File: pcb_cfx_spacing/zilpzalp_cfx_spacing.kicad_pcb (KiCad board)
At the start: 2 copper layers, 205.1 x 102.2 mm, 43 parts, among them SW1 SW_Push, SW10 SW_Push, SW11 SW_Push, SW12 SW_Push, SW13 SW_Push, SW14 SW_Push, SW15 SW_Push, SW16 SW_Push, SW17 SW_Push, SW18 SW_Push, SW19 SW_Push, SW2 SW_Push, SW20 SW_Push, SW21 SW_Push, SW22 SW_Push, SW23 SW_Push, SW24 SW_Push, SW25 SW_Push, SW26 SW_Push, SW27 SW_Push, SW28 SW_Push, SW3 SW_Push, SW4 SW_Push, SW5 SW_Push, SW6 SW_Push, SW7 SW_Push, SW8 SW_Push, SW9 SW_Push, U1 xiao

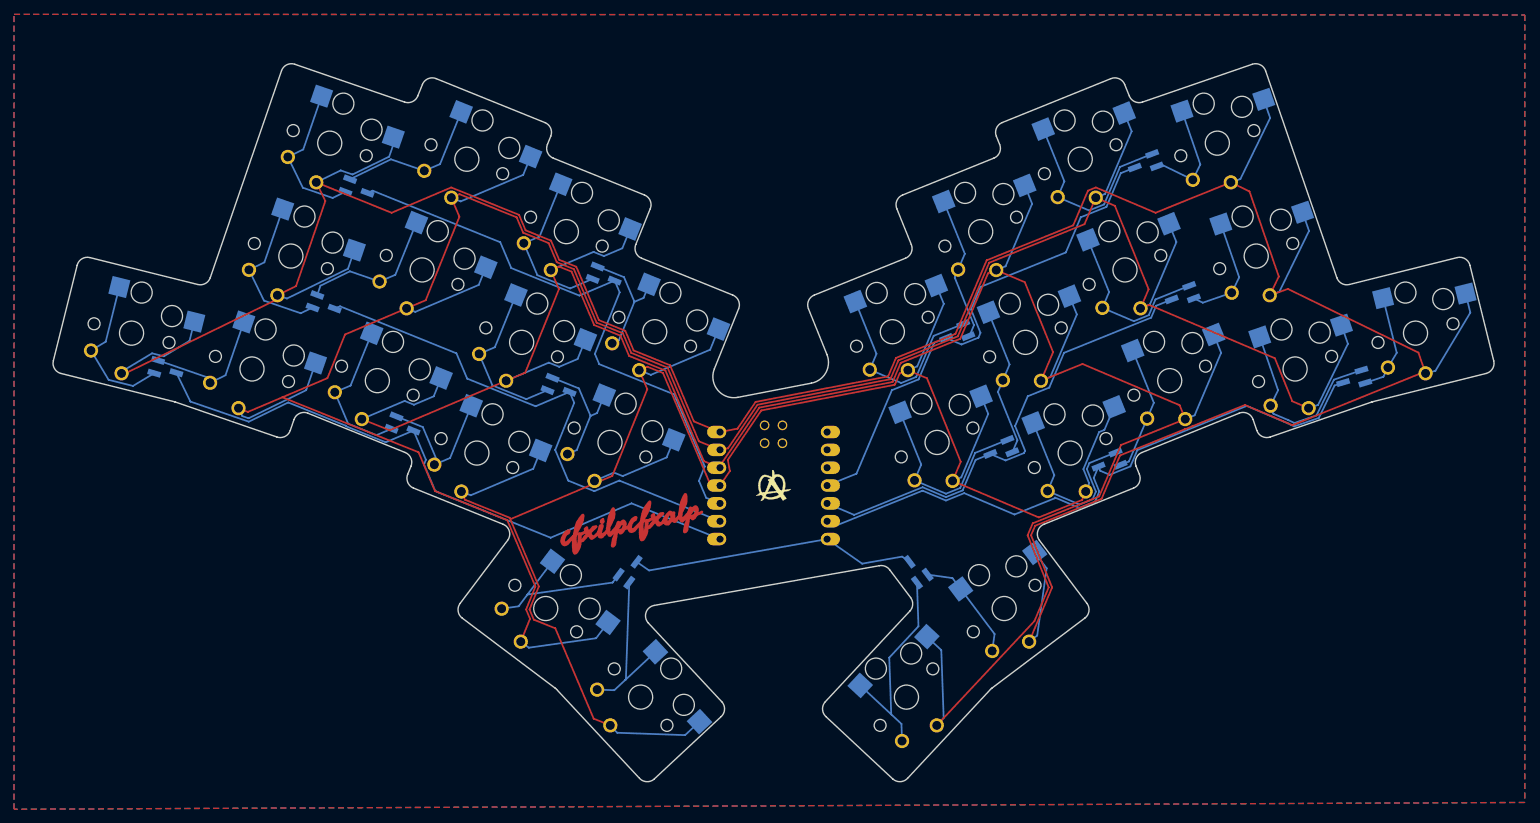
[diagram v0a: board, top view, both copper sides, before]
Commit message: beautify routing slightly
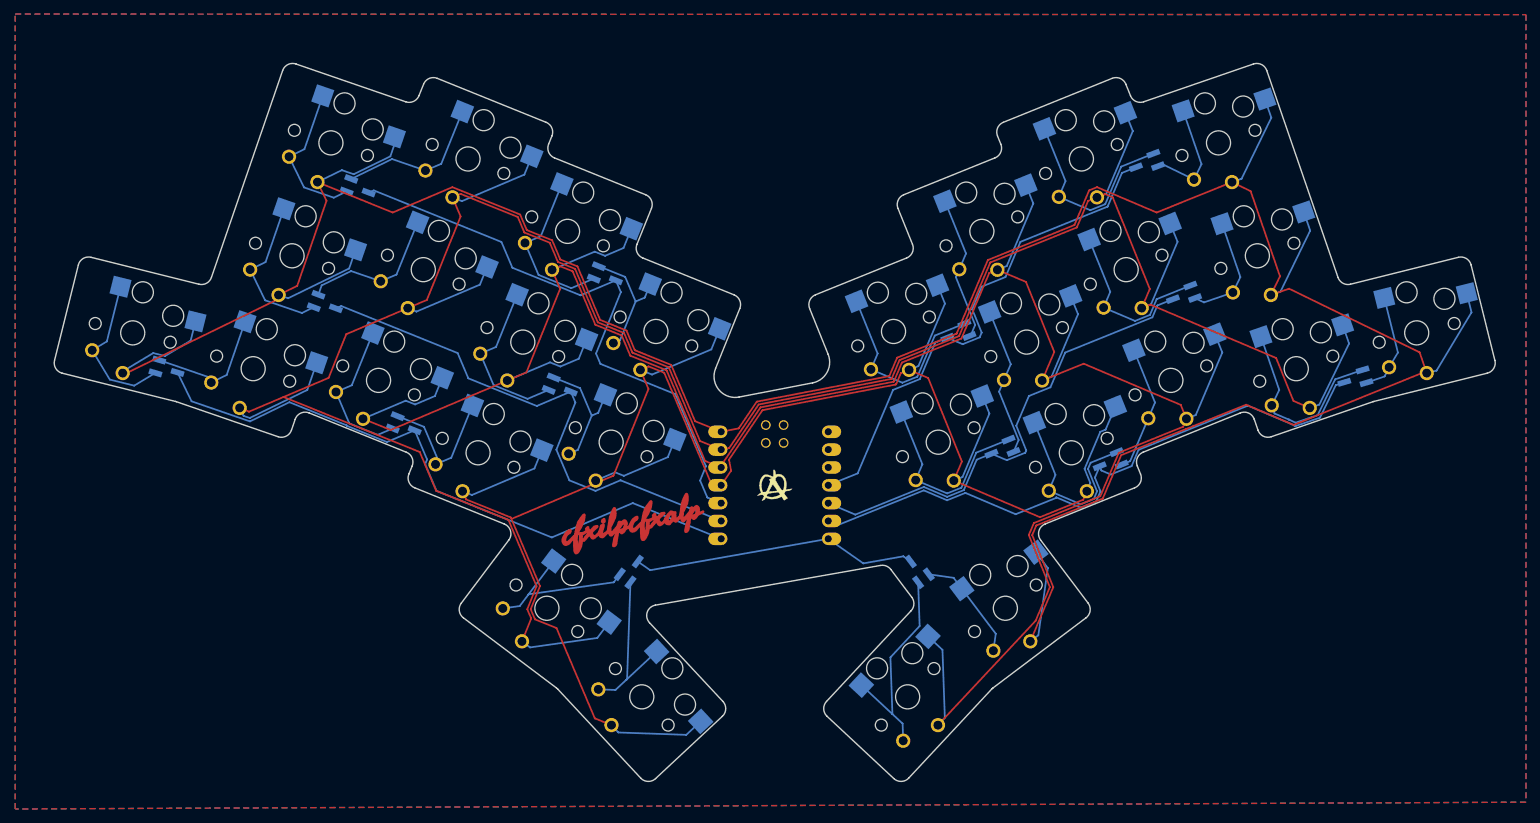
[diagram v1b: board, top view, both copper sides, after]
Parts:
- moved D05 0.17 mm to (122.1, 137.9)
- moved SW10 0.17 mm to (134.3, 137.8)
- moved SW7 0.17 mm to (172.7, 134.0)
- moved SW8 0.17 mm to (185.3, 148.2)
- moved D02 0.17 mm to (184.6, 124.6)
- moved D11 0.17 mm to (240.8, 149.3)
- moved D13 0.17 mm to (234.5, 132.8)
- moved SW1 0.17 mm to (145.4, 105.6)
- moved SW13 0.17 mm to (176.1, 171.9)
- moved SW2 0.17 mm to (164.9, 107.9)
- moved SW3 0.17 mm to (179.1, 118.2)
- moved SW6 0.17 mm to (158.5, 123.7)
- moved SW9 0.17 mm to (117.2, 132.7)
- moved SW26 0.17 mm to (238.1, 118.2)
- moved SW15 0.17 mm to (227.5, 184.5)
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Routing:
- net c2: track 380.5 -> 381.2 mm
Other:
- outline, holes or cut-outs redrawn
